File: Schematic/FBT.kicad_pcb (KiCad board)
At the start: 2 copper layers, 40 x 73.5 mm, 14 parts, among them J1 Battery, J2 Conn_01x04, J3 Conn_01x04, SW1 SW_SPDT, SW2 SW_SPDT

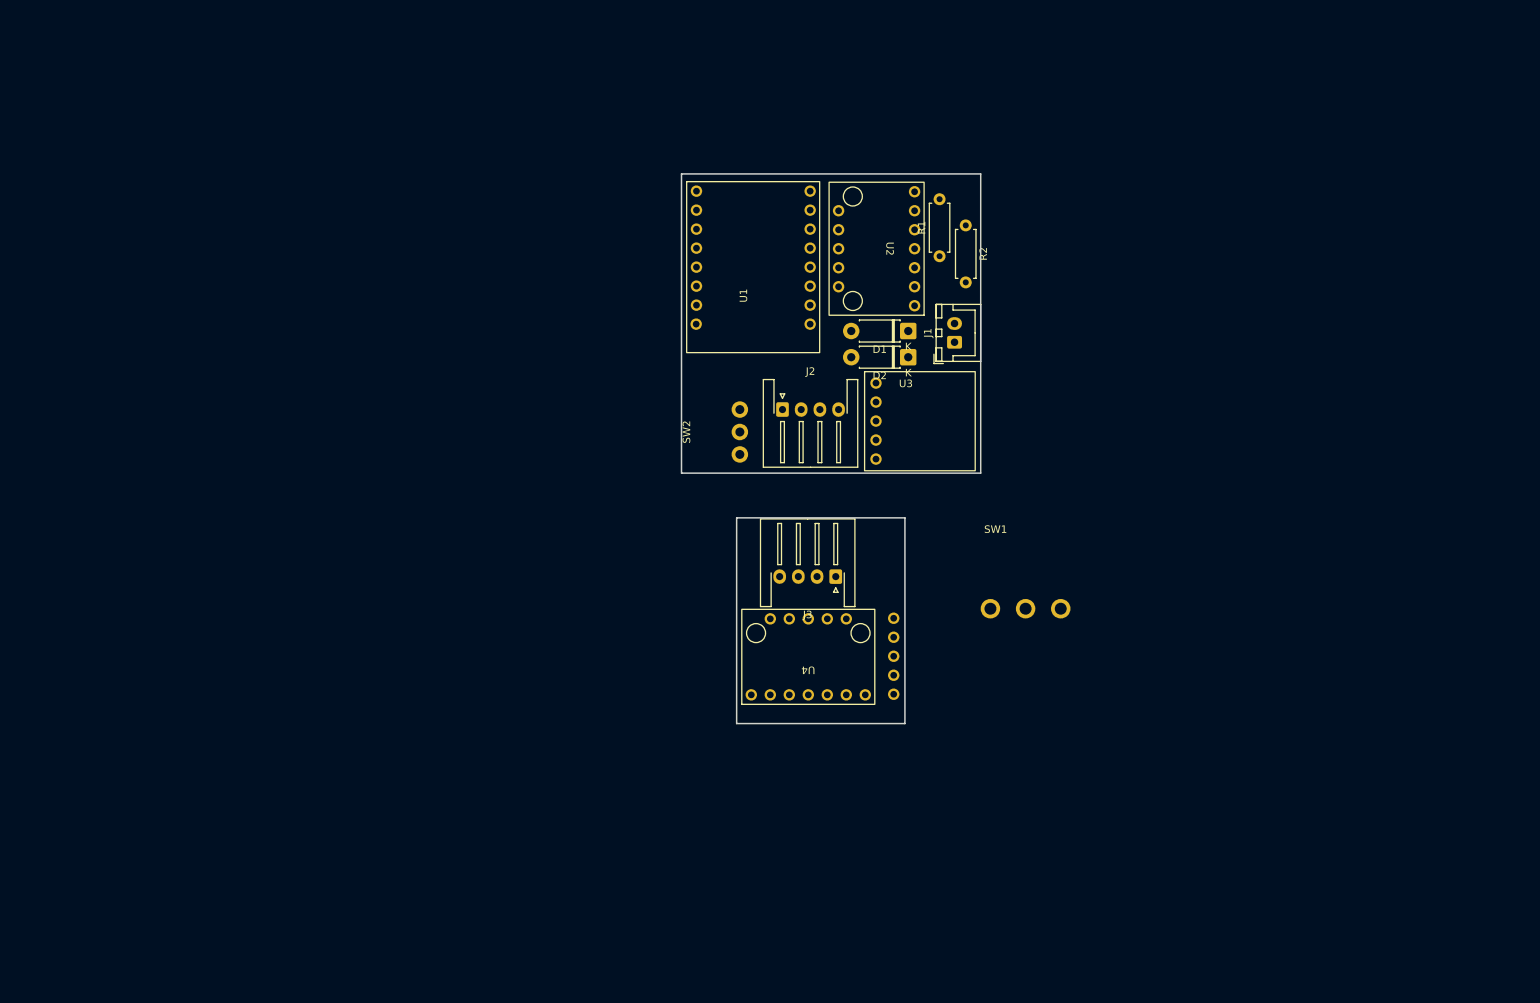
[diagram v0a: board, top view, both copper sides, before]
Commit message: More schematic work
I'm kind of hung up on what charging circuit to use...
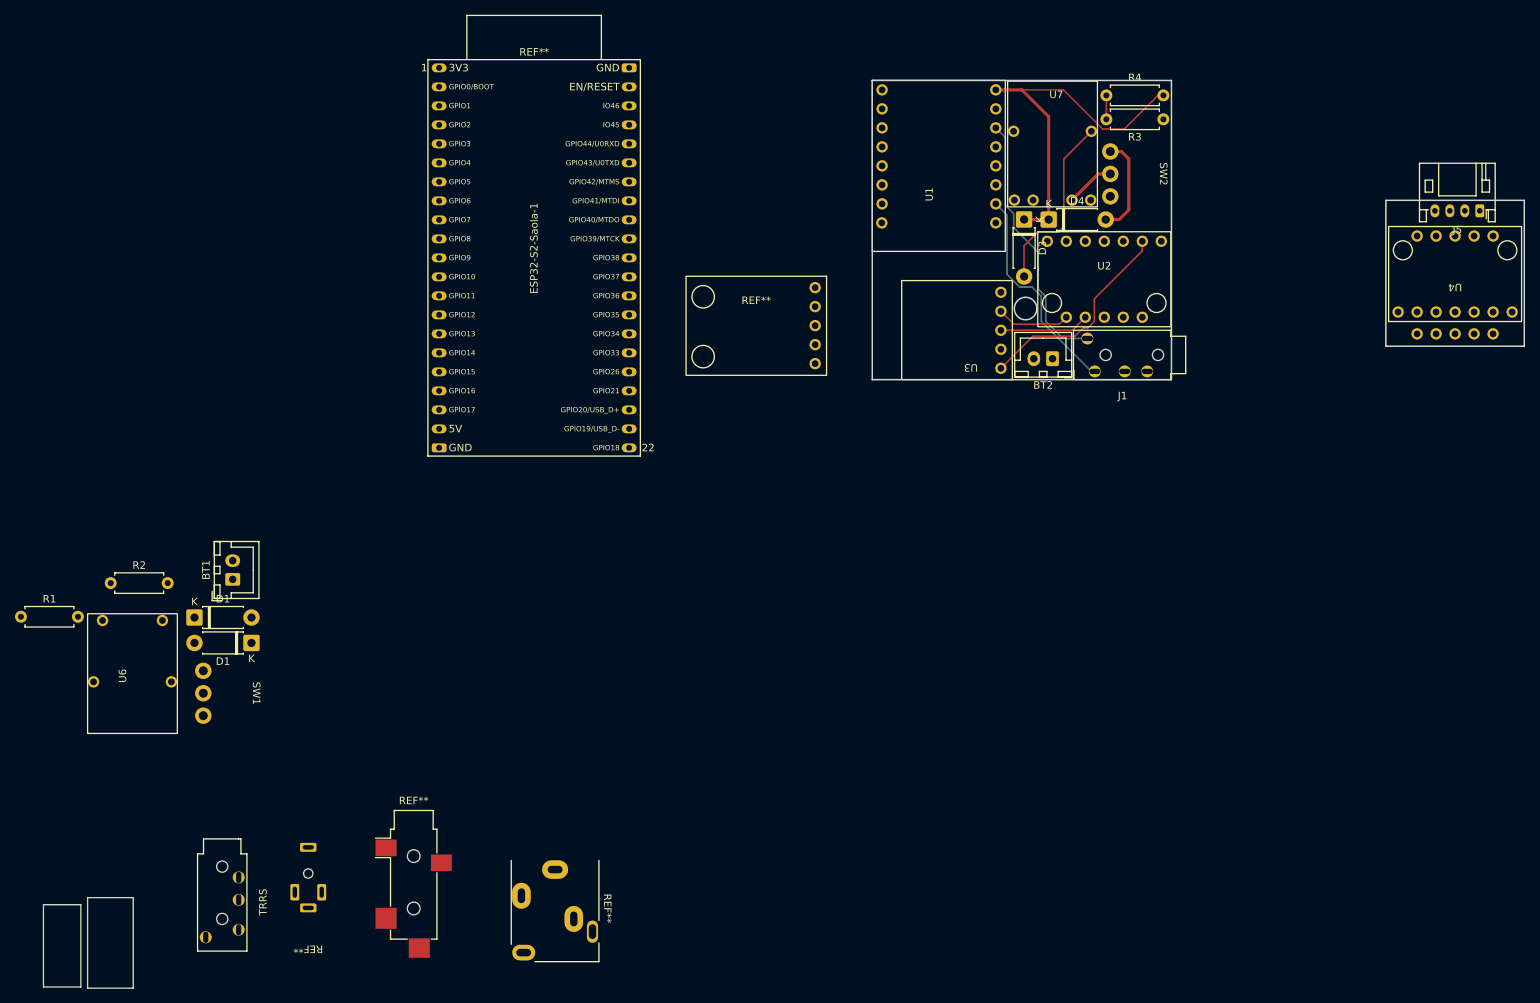
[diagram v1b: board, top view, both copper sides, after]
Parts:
- removed D2: D_Schottky, Diode_THT:D_DO-41_SOD81_P7.62mm_Horizontal
- removed J2, J3: Conn_01x04, Connector_JST:JST_XH_S4B-XH-A-1_1x04_P2.50mm_Horizontal
- added BT1: Battery, Connector_JST:JST_XH_B2B-XH-A_1x02_P2.50mm_Vertical, F.Cu at (44.5, 116.7)
- added BT2: Battery, Connector_JST:JST_XH_B2B-XH-A_1x02_P2.50mm_Vertical, F.Cu at (154.1, 87.2)
- added D1: D_Schottky, Diode_THT:D_DO-41_SOD81_P7.62mm_Horizontal, F.Cu at (47.0, 125.2)
- added D3: D_1N5817 / 4.8v Zener?, Diode_THT:D_DO-41_SOD81_P7.62mm_Horizontal, F.Cu at (150.3, 68.6)
- added D4: D_1N5817, Diode_THT:D_DO-41_SOD81_P7.62mm_Horizontal, F.Cu at (153.6, 68.6)
- added J5: Conn_01x04, Connector_JST:JST_PH_S4B-PH-K_1x04_P2.00mm_Horizontal, F.Cu at (211.2, 67.4)
- added R3: 200K, Resistor_THT:R_Axial_DIN0207_L6.3mm_D2.5mm_P7.62mm_Horizontal, F.Cu at (168.9, 55.2)
- added R4: 200K, Resistor_THT:R_Axial_DIN0207_L6.3mm_D2.5mm_P7.62mm_Horizontal, F.Cu at (161.3, 52.0)
- added REF**: GY-273, My_Library:GY-273, F.Cu at (114.4, 82.9)
- added REF**: Jack_3.5mm_CUI_SJ-3524-SMT_Horizontal, Connector_Audio:Jack_3.5mm_CUI_SJ-3524-SMT_Horizontal, F.Cu at (68.7, 156.2)
- added REF**: PJ-210B, My_Library:PJ-210B, F.Cu at (54.6, 156.0)
- added REF**: ESP32-S2-Saola-1, Espressif:ESP32-S2-Saola-1, F.Cu at (72.1, 48.3)
- added REF**: Jack_3.5mm_CUI_SJ1-3515N_Horizontal, Connector_Audio:Jack_3.5mm_CUI_SJ1-3515N_Horizontal, F.Cu at (87.6, 155.5)
- added TRRS: PJ-320A, My_Library:PJ-320A, F.Cu at (45.3, 151.4)
- added U6: ~, My_Library:LX-LBC3, F.Cu at (25.1, 121.3)
- added U7: ~, My_Library:LX_LBES, F.Cu at (160.1, 66.9)
- D1: value D_Schottky / 4.8 Zener? -> D_Schottky / 4.8v Zener?
- J1: value Battery -> TRRS Connector 3.5; footprint Connector_JST:JST_XH_B2B-XH-A_1x02_P2.50mm_Vertical -> My_Library:PJ-320A
- R1, R2: value 100K -> 200K
- SW1: footprint My_Library:SS12D06 -> My_Library:SS12F21
- moved R1 131.9 mm to (16.2, 121.7), turned to 0 degrees
- moved R2 123.9 mm to (28.2, 117.2), turned to 0 degrees
- moved SW1 105.2 mm to (45.9, 131.9), turned to -90 degrees
- moved D1 102.8 mm to (39.4, 121.8), turned to 0 degrees
- moved U4 100.5 mm to (207.9, 75.9)
- moved U5 93.4 mm to (207.9, 78.9), turned to 90 degrees
- moved SW2 69.3 mm to (167.1, 62.5), turned to -90 degrees
- moved J1 31.2 mm to (171.9, 88.9), turned to 180 degrees
- moved U2 30.7 mm to (161.0, 76.6), turned to -90 degrees
- moved U1 28.3 mm to (138.9, 61.4)
- moved U3 13.9 mm to (142.2, 83.4), turned to 180 degrees
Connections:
- R1 pad 2: ESP32_5V5 -> +BATT
- SW1 pad 2: +BATT -> ESP32_5V5
- SW1 pad 3: unconnected-(SW1-C-Pad3) -> Net-(D1-A)
- SW2 pad 1: unconnected-(SW2-A-Pad1) -> Net-(D4-A)
- SW2 pad 2: unconnected-(SW2-B-Pad2) -> +BATT
- U1 pad 10: unconnected-(U1-D1-Pad10) -> SDA_2
- U1 pad 11: unconnected-(U1-D2-Pad11) -> SCL_1
- U1 pad 12: unconnected-(U1-D3-Pad12) -> SDA_1
- U1 pad 14: unconnected-(U1-3v3-Pad14) -> ESP32_3V3
- U1 pad 4: SDA_1 -> unconnected-(U1-D8-Pad4)
- U1 pad 5: SCL_1 -> unconnected-(U1-D9-Pad5)
- U1 pad 6: SCL_2 -> unconnected-(U1-D10-Pad6)
- U1 pad 7: SDA_2 -> unconnected-(U1-D20/RX-Pad7)
- U1 pad 9: unconnected-(U1-D0-Pad9) -> SCL_2
- U4 pad 1: ESP32_5V5 -> ESP32_3V3
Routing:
- net ESP32_5V5: track 0.00 -> 48.6 mm
- net ESP32_3V3: track 0.00 -> 35.1 mm
- net SDA_2: track 0.00 -> 29.1 mm
- net Net-(U2-3v3): track 0.00 -> 28.5 mm
- net Net-(D3-A): track 0.00 -> 24.7 mm
- net Net-(D4-A): track 0.00 -> 13.3 mm
- net Net-(U2-SCX): track 0.00 -> 12.0 mm
- net Net-(U2-SDX): track 0.00 -> 9.85 mm
- net +BATT: track 0.00 -> 6.57 mm
- net BATTERY_READER: track 0.00 -> 3.20 mm
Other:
- board size 40 x 73.5 mm -> 198 x 121.3 mm

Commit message: work on PCB and shell
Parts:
- removed BT1: Battery, Connector_JST:JST_XH_B2B-XH-A_1x02_P2.50mm_Vertical
- removed D1: D_Schottky / 4.8v Zener?, Diode_THT:D_DO-41_SOD81_P7.62mm_Horizontal
- removed D1: D_Schottky, Diode_THT:D_DO-41_SOD81_P7.62mm_Horizontal
- removed R1, R2: 200K, Resistor_THT:R_Axial_DIN0207_L6.3mm_D2.5mm_P7.62mm_Horizontal
- removed the REF** at (68.7, 156.2)
- removed the REF** at (54.6, 156.0)
- removed the REF** at (72.1, 48.3)
- removed the REF** at (87.6, 155.5)
- removed SW1: SW_SPDT, My_Library:SS12F21
- removed TRRS: PJ-320A, My_Library:PJ-320A
- removed U6: ~, My_Library:LX-LBC3
- moved J5 61.6 mm to (165.6, 108.8)
- moved U4 61.2 mm to (162.6, 117.0), turned to -90 degrees
- moved U5 61.2 mm to (162.6, 120.0)
- moved REF** 40.6 mm to (137.7, 116.2)
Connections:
- U1 pad 10: SDA_2 -> SCL_2
- U1 pad 9: SCL_2 -> SDA_2
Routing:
- net SCL_2: track 0.00 -> 39.3 mm, vias 0 -> 2
- net SCL_1: track 0.00 -> 29.3 mm, vias 0 -> 2
- net +BATT: track 6.57 -> 30.0 mm, vias 0 -> 1
- net SDA_1: track 0.00 -> 19.0 mm, vias 0 -> 1
- net BATTERY_READER: track 3.20 -> 19.5 mm, vias 0 -> 1
- net ESP32_5V5: track 48.6 -> 64.8 mm, vias 0 -> 1
- net Net-(U4-3v3): track 0.00 -> 14.7 mm
- net SDA_2: track 29.1 -> 40.8 mm, vias 0 -> 2
- net ESP32_3V3: track 35.1 -> 41.1 mm, vias 0 -> 2
- net Net-(U4-SDX): track 0.00 -> 3.97 mm
- net Net-(U4-SCX): track 0.00 -> 3.97 mm
- added copper zone on B.Cu, net GND
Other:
- board size 198 x 121.3 mm -> 41.9 x 76.7 mm
- board text added: "+"

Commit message: more tweaks and changes
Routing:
- net +BATT: track 30.0 -> 37.6 mm
- net SCL_2: track 39.3 -> 41.0 mm, vias 2 -> 3
- net ESP32_3V3: track 41.1 -> 40.0 mm
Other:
- outline, holes or cut-outs redrawn

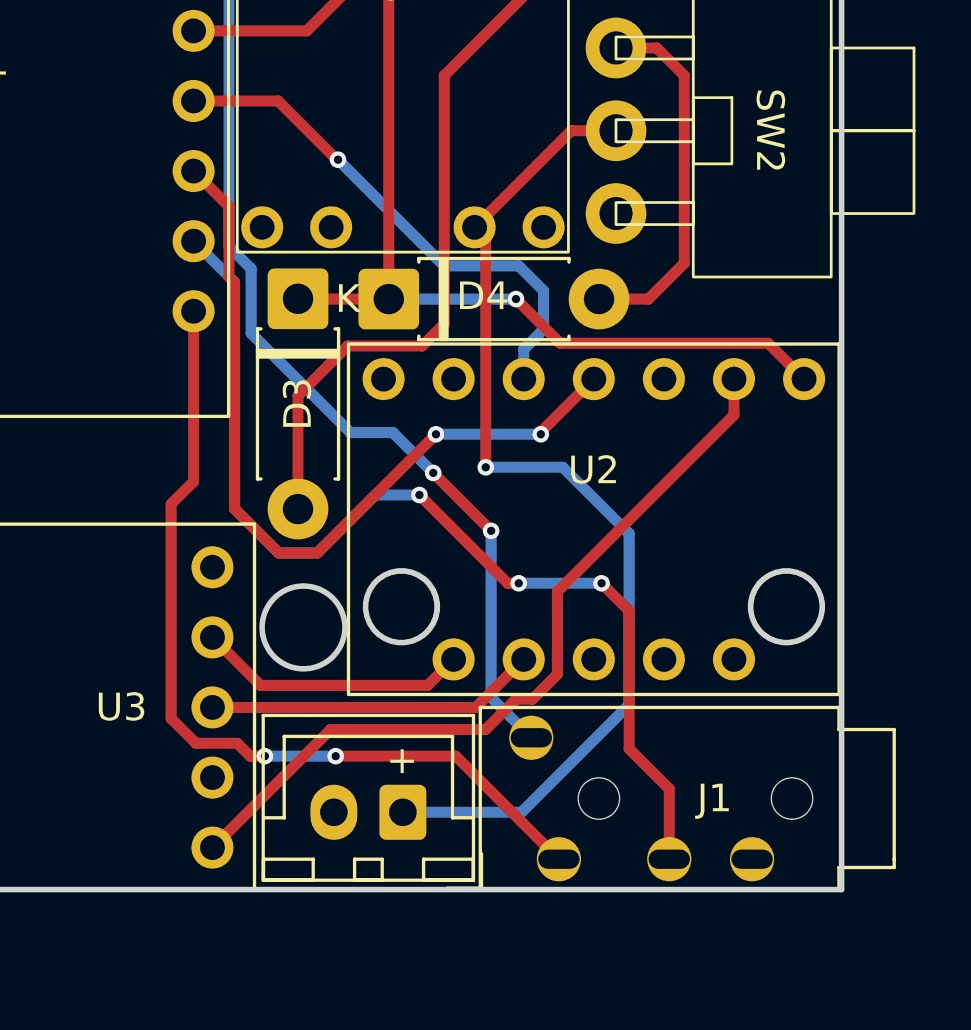
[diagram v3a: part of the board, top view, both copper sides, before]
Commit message: Re-work PCB and add more IMU refs
Trying to make this as dynamic as possible
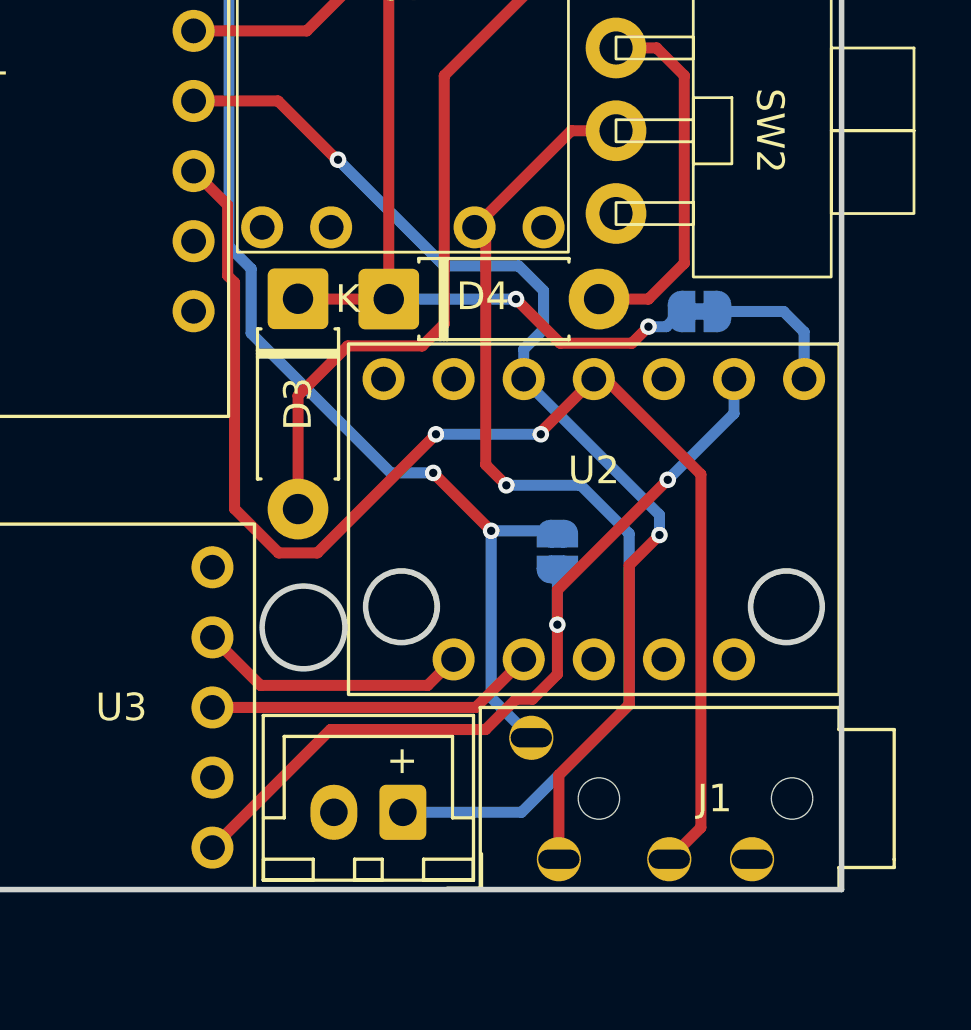
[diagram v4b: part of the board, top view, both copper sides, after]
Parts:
- added JP1: 3v3 in, Jumper:SolderJumper-2_P1.3mm_Open_RoundedPad1.0x1.5mm, B.Cu at (159.7, 77.8)
- added JP2: 5v in, Jumper:SolderJumper-2_P1.3mm_Bridged_RoundedPad1.0x1.5mm, B.Cu at (164.8, 69.0)
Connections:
- J1 pad R1: SDA_2 -> SDA_1
- J1 pad R2: SCL_2 -> SCL_1
- J5 pad 2: SDA_2 -> SDA_1
- J5 pad 3: SCL_2 -> SCL_1
- U1 pad 10: SCL_2 -> unconnected-(U1-D1-Pad10)
- U1 pad 9: SDA_2 -> unconnected-(U1-D0-Pad9)
- U2 pad 1: ESP32_5V5 -> Net-(JP2-A)
- U4 pad 1: ESP32_3V3 -> unconnected-(U4-VIN-Pad1)
- U4 pad 2: Net-(U4-3v3) -> ESP32_3V3
- U4 pad 4: SCL_2 -> SCL_1
- U4 pad 5: SDA_2 -> SDA_1
- U4 pad 7: GND -> unconnected-(U4-SAO-Pad7)
- U5 pad 1: Net-(U4-3v3) -> ESP32_3V3
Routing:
- net SCL_2: track 41.0 -> 0.00 mm, vias 3 -> 0
- net SDA_2: track 40.8 -> 0.00 mm, vias 2 -> 0
- net SDA_1: track 19.0 -> 49.5 mm, vias 1 -> 2
- net SCL_1: track 29.2 -> 52.4 mm
- net ESP32_3V3: track 40.0 -> 57.2 mm
- net Net-(U4-3v3): track 14.7 -> 0.00 mm
- net Net-(JP2-A): track 0.00 -> 5.16 mm
- net ESP32_5V5: track 64.8 -> 60.3 mm, vias 1 -> 2
- net Net-(JP1-B): track 28.5 -> 30.5 mm, vias 0 -> 2
